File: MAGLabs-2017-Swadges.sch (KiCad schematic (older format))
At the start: 31 parts, among them J1 LCD Screen, J2 Valve Magic, J3 Program, U1 ESP12E

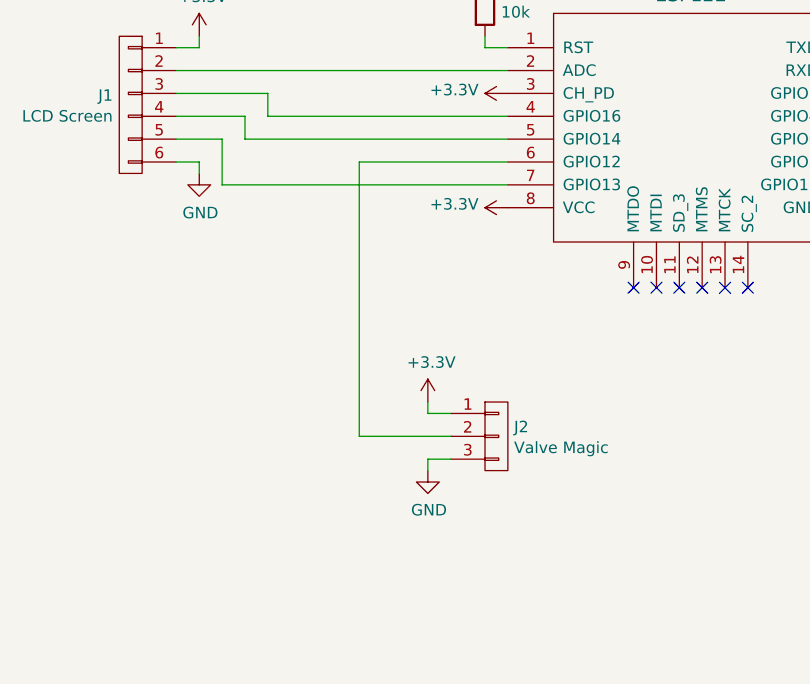
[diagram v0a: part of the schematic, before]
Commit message: Update design with Valve
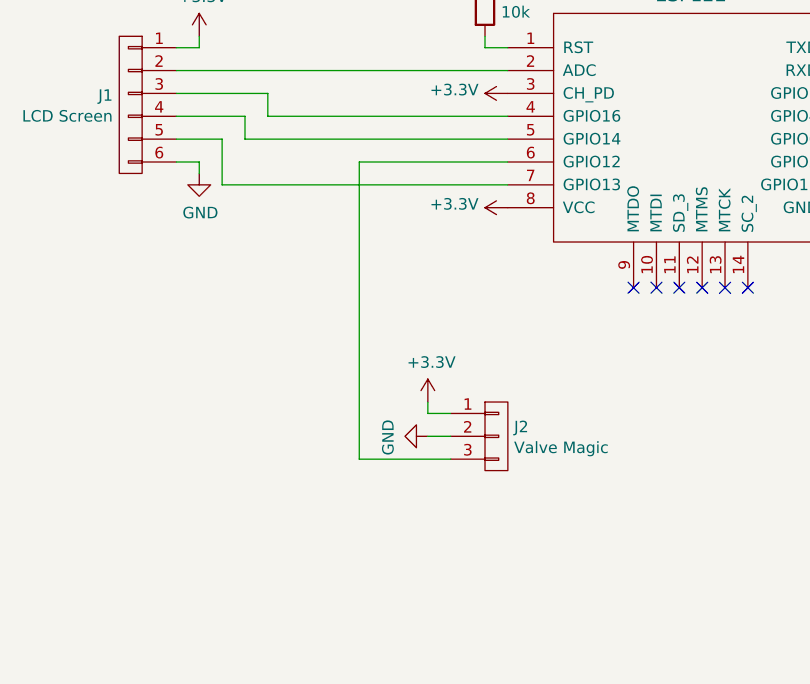
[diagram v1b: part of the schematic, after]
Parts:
- J2: footprint Pin_Headers:Pin_Header_Straight_1x03_Pitch2.54mm_SMD_Pin1Left -> VALVE_CHICKLET_8_1
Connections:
- net GND: now also J2.2 (P2); no longer J2.3 (P3)
- net at U1.6 (GPIO12): now also J2.3 (P3); no longer J2.2 (P2)
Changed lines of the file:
@@
 LIBS:contrib
 LIBS:valves
-LIBS:local
-EELAYER 26 0
+LIBS:MAGLabs-2017-Swadges-cache
+EELAYER 25 0
 EELAYER END
 $Descr A4 11693 8268
@@
 F 0 "J2" H 2527 3391 50  0000 L CNN
 F 1 "Valve Magic" H 2527 3300 50  0000 L CNN
-F 2 "Pin_Headers:Pin_Header_Straight_1x03_Pitch2.54mm_SMD_Pin1Left" H 2450 3350 50  0001 C CNN
+F 2 "VALVE_CHICKLET_8_1" H 2450 3350 50  0001 C CNN
 F 3 "" H 2450 3350 50  0001 C CNN
 	1    2450 3350
@@
 L GND #PWR010
 U 1 1 596F110D
-P 2150 3500
-F 0 "#PWR010" H 2150 3250 50  0001 C CNN
-F 1 "GND" H 2155 3327 50  0000 C CNN
-F 2 "" H 2150 3500 50  0001 C CNN
-F 3 "" H 2150 3500 50  0001 C CNN
-	1    2150 3500
-	1    0    0    -1
-$EndComp
-Wire Wire Line
-	1850 3350 2250 3350
+P 2150 3350
+F 0 "#PWR010" H 2150 3100 50  0001 C CNN
+F 1 "GND" H 2155 3177 50  0000 C CNN
+F 2 "" H 2150 3350 50  0001 C CNN
+F 3 "" H 2150 3350 50  0001 C CNN
+	1    2150 3350
+	0    1    1    0
+$EndComp
 Wire Wire Line
 	2250 3250 2150 3250
@@
 	2150 3250 2150 3200
 Wire Wire Line
-	2250 3450 2150 3450
-Wire Wire Line
-	2150 3450 2150 3500
+	2250 3350 2150 3350
 $Comp
 L +3.3V #PWR011
@@
 	2500 2150 1850 2150
 Wire Wire Line
-	1850 2150 1850 3350
+	1850 2150 1850 3450
 Wire Wire Line
 	1350 2050 2500 2050
@@
 Wire Wire Line
 	1250 2250 2500 2250
+Wire Wire Line
+	1850 3450 2250 3450
 $EndSCHEMATC

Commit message: Now with pullups
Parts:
- added R4, R5, R6: 10k, Resistors_SMD:R_0603, symbol R
- J2: footprint VALVE_CHICKLET_8_1 -> local:VALVE_CHICKLET_8_1
- S1, S2, S3, S4, S5, S6, S7, S8: symbol Tactile_Switch -> Tactile_Switch-RESCUE-MAGLabs-2017-Swadges
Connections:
- net +3V3: now also R4.1, R5.1, R6.1
- net at D1.2 (A), D2.2 (A), D3.1 (K)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: now also R4.2
- net at S3.2, U1.19 (GPIO4): now also R5.2
- net at S1.1, U1.20 (GPIO5): now also R6.2
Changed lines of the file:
@@
 EESchema Schematic File Version 2
+LIBS:MAGLabs-2017-Swadges-rescue
 LIBS:power
 LIBS:device
@@
 LIBS:contrib
 LIBS:valves
+LIBS:local
 LIBS:MAGLabs-2017-Swadges-cache
-EELAYER 25 0
+EELAYER 26 0
 EELAYER END
 $Descr A4 11693 8268
@@
 $EndComp
 $Comp
-L Tactile_Switch S1
+L Tactile_Switch-RESCUE-MAGLabs-2017-Swadges S1
 U 1 1 596EC645
 P 6150 950
@@
 $EndComp
 $Comp
-L Tactile_Switch S2
+L Tactile_Switch-RESCUE-MAGLabs-2017-Swadges S2
 U 1 1 596EC831
 P 6600 950
@@
 $EndComp
 $Comp
-L Tactile_Switch S3
+L Tactile_Switch-RESCUE-MAGLabs-2017-Swadges S3
 U 1 1 596EC875
 P 6150 2250
@@
 $EndComp
 $Comp
-L Tactile_Switch S4
+L Tactile_Switch-RESCUE-MAGLabs-2017-Swadges S4
 U 1 1 596EC8B5
 P 6600 2250
@@
 $EndComp
 $Comp
-L Tactile_Switch S5
+L Tactile_Switch-RESCUE-MAGLabs-2017-Swadges S5
 U 1 1 596EC995
 P 7100 1600
@@
 $EndComp
 $Comp
-L Tactile_Switch S6
+L Tactile_Switch-RESCUE-MAGLabs-2017-Swadges S6
 U 1 1 596EC9D7
 P 7550 1600
@@
 $EndComp
 $Comp
-L Tactile_Switch S7
+L Tactile_Switch-RESCUE-MAGLabs-2017-Swadges S7
 U 1 1 596ECA1D
 P 9900 1750
@@
 $EndComp
 $Comp
-L Tactile_Switch S8
+L Tactile_Switch-RESCUE-MAGLabs-2017-Swadges S8
 U 1 1 596ECA67
 P 10450 1750
@@
 F 0 "J2" H 2527 3391 50  0000 L CNN
 F 1 "Valve Magic" H 2527 3300 50  0000 L CNN
-F 2 "VALVE_CHICKLET_8_1" H 2450 3350 50  0001 C CNN
+F 2 "local:VALVE_CHICKLET_8_1" H 2450 3350 50  0001 C CNN
 F 3 "" H 2450 3350 50  0001 C CNN
 	1    2450 3350
@@
 Wire Wire Line
 	1850 3450 2250 3450
+$Comp
+L R R4
+U 1 1 59703F15
+P 4700 1600
+F 0 "R4" H 4770 1646 50  0000 L CNN
+F 1 "10k" H 4770 1555 50  0000 L CNN
+F 2 "Resistors_SMD:R_0603" V 4630 1600 50  0001 C CNN
+F 3 "" H 4700 1600 50  0001 C CNN
+	1    4700 1600
+	1    0    0    -1
+$EndComp
+$Comp
+L R R5
+U 1 1 59703F91
+P 4900 1600
+F 0 "R5" H 4970 1646 50  0000 L CNN
+F 1 "10k" H 4970 1555 50  0000 L CNN
+F 2 "Resistors_SMD:R_0603" V 4830 1600 50  0001 C CNN
+F 3 "" H 4900 1600 50  0001 C CNN
+	1    4900 1600
+	1    0    0    -1
+$EndComp
+$Comp
+L R R6
+U 1 1 59703FEB
+P 5100 1600
+F 0 "R6" H 5170 1646 50  0000 L CNN
+F 1 "10k" H 5170 1555 50  0000 L CNN
+F 2 "Resistors_SMD:R_0603" V 5030 1600 50  0001 C CNN
+F 3 "" H 5100 1600 50  0001 C CNN
+	1    5100 1600
+	1    0    0    -1
+$EndComp
+Wire Wire Line
+	4700 2250 4700 1750
+Connection ~ 4700 2250
+Wire Wire Line
+	4900 1750 4900 1950
+Connection ~ 4900 1950
+Wire Wire Line
+	5100 1750 5100 1850
+Connection ~ 5100 1850
+$Comp
+L +3.3V #PWR027
+U 1 1 597041F5
+P 4700 1450
+F 0 "#PWR027" H 4700 1300 50  0001 C CNN
+F 1 "+3.3V" H 4715 1623 50  0000 C CNN
+F 2 "" H 4700 1450 50  0001 C CNN
+F 3 "" H 4700 1450 50  0001 C CNN
+	1    4700 1450
+	1    0    0    -1
+$EndComp
+$Comp
+L +3.3V #PWR028
+U 1 1 5970424B
+P 4900 1450
+F 0 "#PWR028" H 4900 1300 50  0001 C CNN
+F 1 "+3.3V" H 4915 1623 50  0000 C CNN
+F 2 "" H 4900 1450 50  0001 C CNN
+F 3 "" H 4900 1450 50  0001 C CNN
+	1    4900 1450
+	1    0    0    -1
+$EndComp
+$Comp
+L +3.3V #PWR029
+U 1 1 5970429A
+P 5100 1450
+F 0 "#PWR029" H 5100 1300 50  0001 C CNN
+F 1 "+3.3V" H 5115 1623 50  0000 C CNN
+F 2 "" H 5100 1450 50  0001 C CNN
+F 3 "" H 5100 1450 50  0001 C CNN
+	1    5100 1450
+	1    0    0    -1
+$EndComp
 $EndSCHEMATC

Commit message: Update design
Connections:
- net GPIO0: now also R3.2
- net at S8.1, U1.17 (GPIO2): now also R2.2
- net at S7.2: no longer R2.2
- net at S8.2: no longer R3.2
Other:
- moved on the sheet: R2, R3, R4, R5, R6
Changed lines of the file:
@@
 LIBS:contrib
 LIBS:valves
-LIBS:local
 LIBS:MAGLabs-2017-Swadges-cache
-EELAYER 26 0
+EELAYER 25 0
 EELAYER END
 $Descr A4 11693 8268
@@
 L R R2
 U 1 1 596F08C9
-P 9550 1250
-F 0 "R2" H 9620 1296 50  0000 L CNN
-F 1 "10k" H 9620 1205 50  0000 L CNN
-F 2 "Resistors_SMD:R_0603" V 9480 1250 50  0001 C CNN
-F 3 "" H 9550 1250 50  0001 C CNN
-	1    9550 1250
+P 8100 2300
+F 0 "R2" H 8170 2346 50  0000 L CNN
+F 1 "10k" H 8170 2255 50  0000 L CNN
+F 2 "Resistors_SMD:R_0603" V 8030 2300 50  0001 C CNN
+F 3 "" H 8100 2300 50  0001 C CNN
+	1    8100 2300
 	1    0    0    -1
 $EndComp
@@
 L R R3
 U 1 1 596F092F
-P 10100 1250
-F 0 "R3" H 10170 1296 50  0000 L CNN
-F 1 "10k" H 10170 1205 50  0000 L CNN
-F 2 "Resistors_SMD:R_0603" V 10030 1250 50  0001 C CNN
-F 3 "" H 10100 1250 50  0001 C CNN
-	1    10100 1250
+P 8650 2300
+F 0 "R3" H 8720 2346 50  0000 L CNN
+F 1 "10k" H 8720 2255 50  0000 L CNN
+F 2 "Resistors_SMD:R_0603" V 8580 2300 50  0001 C CNN
+F 3 "" H 8650 2300 50  0001 C CNN
+	1    8650 2300
 	1    0    0    -1
 $EndComp
@@
 L +3.3V #PWR05
 U 1 1 596F0986
-P 9550 1100
-F 0 "#PWR05" H 9550 950 50  0001 C CNN
-F 1 "+3.3V" H 9565 1273 50  0000 C CNN
-F 2 "" H 9550 1100 50  0001 C CNN
-F 3 "" H 9550 1100 50  0001 C CNN
-	1    9550 1100
+P 8100 2150
+F 0 "#PWR05" H 8100 2000 50  0001 C CNN
+F 1 "+3.3V" H 8115 2323 50  0000 C CNN
+F 2 "" H 8100 2150 50  0001 C CNN
+F 3 "" H 8100 2150 50  0001 C CNN
+	1    8100 2150
 	1    0    0    -1
 $EndComp
@@
 L +3.3V #PWR06
 U 1 1 596F09B4
-P 10100 1100
-F 0 "#PWR06" H 10100 950 50  0001 C CNN
-F 1 "+3.3V" H 10115 1273 50  0000 C CNN
-F 2 "" H 10100 1100 50  0001 C CNN
-F 3 "" H 10100 1100 50  0001 C CNN
-	1    10100 1100
+P 8650 2150
+F 0 "#PWR06" H 8650 2000 50  0001 C CNN
+F 1 "+3.3V" H 8665 2323 50  0000 C CNN
+F 2 "" H 8650 2150 50  0001 C CNN
+F 3 "" H 8650 2150 50  0001 C CNN
+	1    8650 2150
 	1    0    0    -1
 $EndComp
@@
 L R R4
 U 1 1 59703F15
-P 4700 1600
-F 0 "R4" H 4770 1646 50  0000 L CNN
-F 1 "10k" H 4770 1555 50  0000 L CNN
-F 2 "Resistors_SMD:R_0603" V 4630 1600 50  0001 C CNN
-F 3 "" H 4700 1600 50  0001 C CNN
-	1    4700 1600
+P 4700 1500
+F 0 "R4" H 4770 1546 50  0000 L CNN
+F 1 "10k" H 4770 1455 50  0000 L CNN
+F 2 "Resistors_SMD:R_0603" V 4630 1500 50  0001 C CNN
+F 3 "" H 4700 1500 50  0001 C CNN
+	1    4700 1500
 	1    0    0    -1
 $EndComp
@@
 L R R5
 U 1 1 59703F91
-P 4900 1600
-F 0 "R5" H 4970 1646 50  0000 L CNN
-F 1 "10k" H 4970 1555 50  0000 L CNN
-F 2 "Resistors_SMD:R_0603" V 4830 1600 50  0001 C CNN
-F 3 "" H 4900 1600 50  0001 C CNN
-	1    4900 1600
+P 4900 1500
+F 0 "R5" H 4970 1546 50  0000 L CNN
+F 1 "10k" H 4970 1455 50  0000 L CNN
+F 2 "Resistors_SMD:R_0603" V 4830 1500 50  0001 C CNN
+F 3 "" H 4900 1500 50  0001 C CNN
+	1    4900 1500
 	1    0    0    -1
 $EndComp
@@
 L R R6
 U 1 1 59703FEB
-P 5100 1600
-F 0 "R6" H 5170 1646 50  0000 L CNN
-F 1 "10k" H 5170 1555 50  0000 L CNN
-F 2 "Resistors_SMD:R_0603" V 5030 1600 50  0001 C CNN
-F 3 "" H 5100 1600 50  0001 C CNN
-	1    5100 1600
-	1    0    0    -1
-$EndComp
-Wire Wire Line
-	4700 2250 4700 1750
+P 5100 1500
+F 0 "R6" H 5170 1546 50  0000 L CNN
+F 1 "10k" H 5170 1455 50  0000 L CNN
+F 2 "Resistors_SMD:R_0603" V 5030 1500 50  0001 C CNN
+F 3 "" H 5100 1500 50  0001 C CNN
+	1    5100 1500
+	1    0    0    -1
+$EndComp
+Wire Wire Line
+	4700 1650 4700 2250
 Connection ~ 4700 2250
 Wire Wire Line
-	4900 1750 4900 1950
+	4900 1650 4900 1950
 Connection ~ 4900 1950
 Wire Wire Line
-	5100 1750 5100 1850
+	5100 1650 5100 1850
 Connection ~ 5100 1850
 $Comp
 L +3.3V #PWR027
 U 1 1 597041F5
-P 4700 1450
-F 0 "#PWR027" H 4700 1300 50  0001 C CNN
-F 1 "+3.3V" H 4715 1623 50  0000 C CNN
-F 2 "" H 4700 1450 50  0001 C CNN
-F 3 "" H 4700 1450 50  0001 C CNN
-	1    4700 1450
+P 4700 1350
+F 0 "#PWR027" H 4700 1200 50  0001 C CNN
+F 1 "+3.3V" H 4715 1523 50  0000 C CNN
+F 2 "" H 4700 1350 50  0001 C CNN
+F 3 "" H 4700 1350 50  0001 C CNN
+	1    4700 1350
 	1    0    0    -1
 $EndComp
@@
 L +3.3V #PWR028
 U 1 1 5970424B
-P 4900 1450
-F 0 "#PWR028" H 4900 1300 50  0001 C CNN
-F 1 "+3.3V" H 4915 1623 50  0000 C CNN
-F 2 "" H 4900 1450 50  0001 C CNN
-F 3 "" H 4900 1450 50  0001 C CNN
-	1    4900 1450
+P 4900 1350
+F 0 "#PWR028" H 4900 1200 50  0001 C CNN
+F 1 "+3.3V" H 4915 1523 50  0000 C CNN
+F 2 "" H 4900 1350 50  0001 C CNN
+F 3 "" H 4900 1350 50  0001 C CNN
+	1    4900 1350
 	1    0    0    -1
 $EndComp
@@
 L +3.3V #PWR029
 U 1 1 5970429A
-P 5100 1450
-F 0 "#PWR029" H 5100 1300 50  0001 C CNN
-F 1 "+3.3V" H 5115 1623 50  0000 C CNN
-F 2 "" H 5100 1450 50  0001 C CNN
-F 3 "" H 5100 1450 50  0001 C CNN
-	1    5100 1450
-	1    0    0    -1
-$EndComp
+P 5100 1350
+F 0 "#PWR029" H 5100 1200 50  0001 C CNN
+F 1 "+3.3V" H 5115 1523 50  0000 C CNN
+F 2 "" H 5100 1350 50  0001 C CNN
+F 3 "" H 5100 1350 50  0001 C CNN
+	1    5100 1350
+	1    0    0    -1
+$EndComp
+Wire Wire Line
+	8650 2450 8650 2800
+Wire Wire Line
+	8100 2450 8100 2900
+Connection ~ 8650 2800
+Connection ~ 8100 2900
 $EndSCHEMATC

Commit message: Updated schematic
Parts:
- added R7: 10k, Resistors_SMD:R_0603, symbol R
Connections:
- net +3V3: now also R7.1; no longer R4.1
- net GND: now also R4.1
- net at D1.2 (A), D2.2 (A), D3.1 (K)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: now also J1.3 (P3), U1.4 (GPIO16), R7.2; no longer R4.2, U1.16 (GPIO15)
- new net: R4.2, U1.16 (GPIO15)
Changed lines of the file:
@@
 Wire Wire Line
 	5800 1850 4100 1850
-Wire Wire Line
-	5650 1600 5650 2250
-Wire Wire Line
-	5650 2250 4100 2250
 Connection ~ 6050 1600
 Wire Wire Line
@@
 Wire Wire Line
 	4700 1650 4700 2250
-Connection ~ 4700 2250
 Wire Wire Line
 	4900 1650 4900 1950
@@
 $Comp
 L +3.3V #PWR027
-U 1 1 597041F5
-P 4700 1350
-F 0 "#PWR027" H 4700 1200 50  0001 C CNN
-F 1 "+3.3V" H 4715 1523 50  0000 C CNN
-F 2 "" H 4700 1350 50  0001 C CNN
-F 3 "" H 4700 1350 50  0001 C CNN
-	1    4700 1350
-	1    0    0    -1
-$EndComp
-$Comp
-L +3.3V #PWR028
 U 1 1 5970424B
 P 4900 1350
-F 0 "#PWR028" H 4900 1200 50  0001 C CNN
+F 0 "#PWR027" H 4900 1200 50  0001 C CNN
 F 1 "+3.3V" H 4915 1523 50  0000 C CNN
 F 2 "" H 4900 1350 50  0001 C CNN
@@
 $EndComp
 $Comp
-L +3.3V #PWR029
+L +3.3V #PWR028
 U 1 1 5970429A
 P 5100 1350
-F 0 "#PWR029" H 5100 1200 50  0001 C CNN
+F 0 "#PWR028" H 5100 1200 50  0001 C CNN
 F 1 "+3.3V" H 5115 1523 50  0000 C CNN
 F 2 "" H 5100 1350 50  0001 C CNN
@@
 Connection ~ 8650 2800
 Connection ~ 8100 2900
+$Comp
+L GND #PWR029
+U 1 1 597EDCC0
+P 4700 1350
+F 0 "#PWR029" H 4700 1100 50  0001 C CNN
+F 1 "GND" H 4700 1200 50  0000 C CNN
+F 2 "" H 4700 1350 50  0001 C CNN
+F 3 "" H 4700 1350 50  0001 C CNN
+	1    4700 1350
+	-1   0    0    1
+$EndComp
+Wire Wire Line
+	4700 2250 4100 2250
+Wire Wire Line
+	5650 1600 5650 950
+Wire Wire Line
+	5650 950  1950 950
+Wire Wire Line
+	1950 950  1950 1950
+Connection ~ 1950 1950
+$Comp
+L R R7
+U 1 1 597EE5FD
+P 1800 1100
+F 0 "R7" V 1880 1100 50  0000 C CNN
+F 1 "10k" V 1800 1100 50  0000 C CNN
+F 2 "Resistors_SMD:R_0603" V 1730 1100 50  0001 C CNN
+F 3 "" H 1800 1100 50  0001 C CNN
+	1    1800 1100
+	1    0    0    -1
+$EndComp
+$Comp
+L +3.3V #PWR030
+U 1 1 597EE66C
+P 1800 950
+F 0 "#PWR030" H 1800 800 50  0001 C CNN
+F 1 "+3.3V" H 1800 1090 50  0000 C CNN
+F 2 "" H 1800 950 50  0001 C CNN
+F 3 "" H 1800 950 50  0001 C CNN
+	1    1800 950
+	1    0    0    -1
+$EndComp
+Wire Wire Line
+	1800 1250 1800 1300
+Wire Wire Line
+	1800 1300 1950 1300
+Connection ~ 1950 1300
 $EndSCHEMATC

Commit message: Pre route
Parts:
- BT1, BT2: footprint local:BK-53 -> local:Elecrow-ThroughHole-AA-Battery
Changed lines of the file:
@@
 LIBS:contrib
 LIBS:valves
+LIBS:local
 LIBS:MAGLabs-2017-Swadges-cache
-EELAYER 25 0
+EELAYER 26 0
 EELAYER END
 $Descr A4 11693 8268
@@
 F 0 "BT1" H 1218 6946 50  0000 L CNN
 F 1 "Battery_Cell" H 1218 6855 50  0000 L CNN
-F 2 "local:BK-53" V 1100 6910 50  0001 C CNN
+F 2 "local:Elecrow-ThroughHole-AA-Battery" V 1100 6910 50  0001 C CNN
 F 3 "" V 1100 6910 50  0001 C CNN
 	1    1100 6850
@@
 F 0 "BT2" H 1218 7346 50  0000 L CNN
 F 1 "Battery_Cell" H 1218 7255 50  0000 L CNN
-F 2 "local:BK-53" V 1100 7310 50  0001 C CNN
+F 2 "local:Elecrow-ThroughHole-AA-Battery" V 1100 7310 50  0001 C CNN
 F 3 "" V 1100 7310 50  0001 C CNN
 	1    1100 7250
